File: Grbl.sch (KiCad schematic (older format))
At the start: 19 parts, among them P1 CTL, P2 MISC, P3 STEP, P4 SPIN, P5 LIMIT

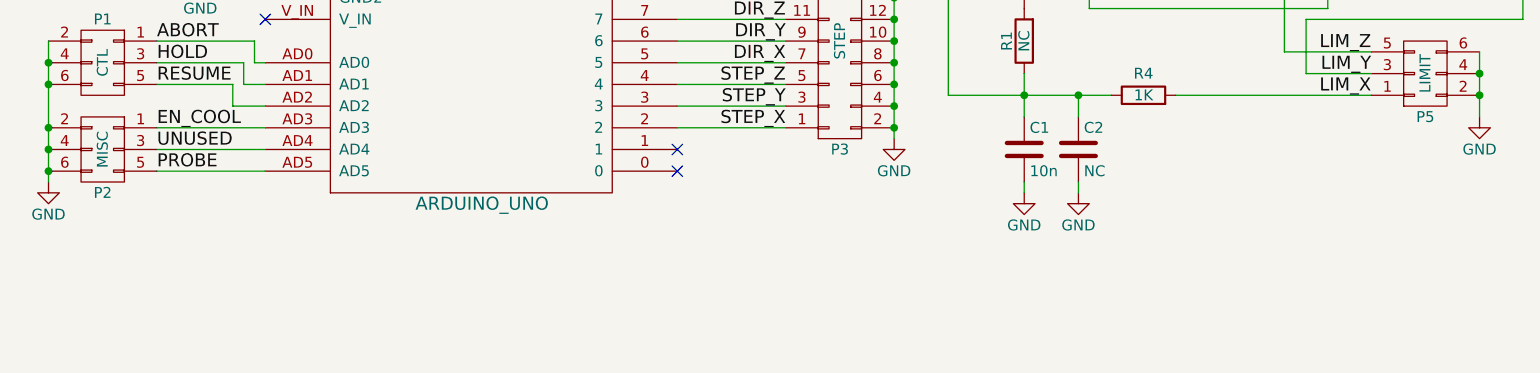
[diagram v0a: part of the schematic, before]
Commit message: Add more ground pins
This helps connecting the shield wire of cables.
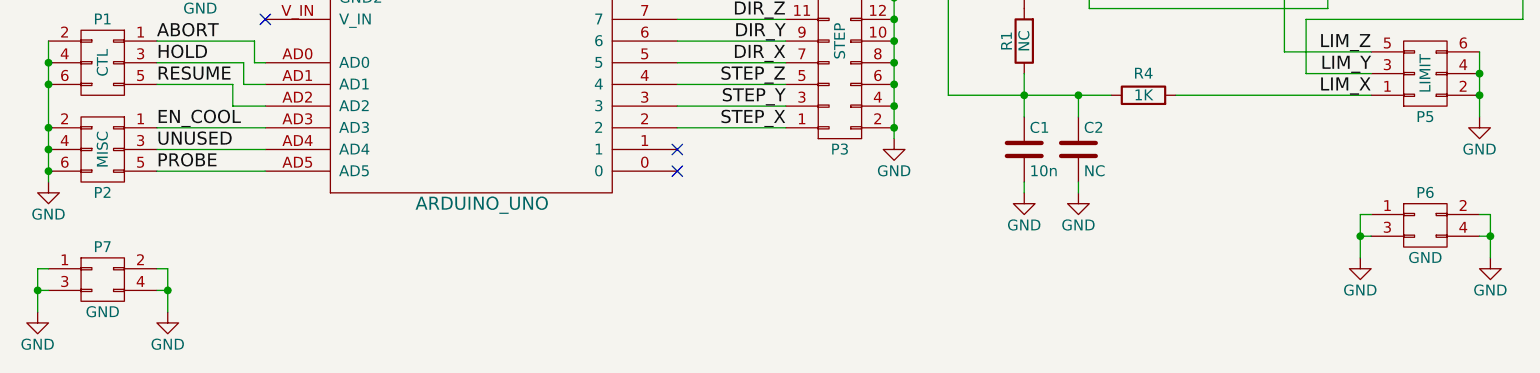
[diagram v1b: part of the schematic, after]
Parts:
- added P6, P7: GND, Pin_Headers:Pin_Header_Straight_2x02, symbol CONN_02X02
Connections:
- net GND: now also P6.1 (P1), P6.2 (P2), P6.3 (P3), P6.4 (P4), P7.1 (P1), P7.2 (P2), P7.3 (P3), P7.4 (P4)
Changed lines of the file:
@@
 NoConn ~ 5750 3300
 $Comp
-L GND #PWR?
+L GND #PWR016
 U 1 1 5638B3BA
 P 5650 1400
-F 0 "#PWR?" H 5650 1150 50  0001 C CNN
+F 0 "#PWR016" H 5650 1150 50  0001 C CNN
 F 1 "GND" H 5650 1250 50  0000 C CNN
 F 2 "" H 5650 1400 60  0000 C CNN
@@
 	3750 2500 3750 2400
 Connection ~ 3750 2400
+$Comp
+L CONN_02X02 P7
+U 1 1 595F1AB2
+P 3100 3800
+F 0 "P7" H 3100 3950 50  0000 C CNN
+F 1 "GND" H 3100 3650 50  0000 C CNN
+F 2 "Pin_Headers:Pin_Header_Straight_2x02" H 3100 2600 50  0001 C CNN
+F 3 "" H 3100 2600 50  0001 C CNN
+	1    3100 3800
+	1    0    0    -1
+$EndComp
+$Comp
+L GND #PWR017
+U 1 1 595F1C99
+P 3400 3950
+F 0 "#PWR017" H 3400 3700 50  0001 C CNN
+F 1 "GND" H 3400 3800 50  0000 C CNN
+F 2 "" H 3400 3950 60  0000 C CNN
+F 3 "" H 3400 3950 60  0000 C CNN
+	1    3400 3950
+	1    0    0    -1
+$EndComp
+$Comp
+L GND #PWR018
+U 1 1 595F1CE0
+P 2800 3950
+F 0 "#PWR018" H 2800 3700 50  0001 C CNN
+F 1 "GND" H 2800 3800 50  0000 C CNN
+F 2 "" H 2800 3950 60  0000 C CNN
+F 3 "" H 2800 3950 60  0000 C CNN
+	1    2800 3950
+	1    0    0    -1
+$EndComp
+Wire Wire Line
+	2800 3750 2800 3950
+Wire Wire Line
+	2800 3850 2850 3850
+Wire Wire Line
+	2800 3750 2850 3750
+Connection ~ 2800 3850
+Wire Wire Line
+	3350 3850 3400 3850
+Wire Wire Line
+	3400 3750 3400 3950
+Wire Wire Line
+	3350 3750 3400 3750
+Connection ~ 3400 3850
+$Comp
+L CONN_02X02 P6
+U 1 1 595F38E7
+P 9200 3550
+F 0 "P6" H 9200 3700 50  0000 C CNN
+F 1 "GND" H 9200 3400 50  0000 C CNN
+F 2 "Pin_Headers:Pin_Header_Straight_2x02" H 9200 2350 50  0001 C CNN
+F 3 "" H 9200 2350 50  0001 C CNN
+	1    9200 3550
+	1    0    0    -1
+$EndComp
+$Comp
+L GND #PWR?
+U 1 1 595F38ED
+P 9500 3700
+F 0 "#PWR?" H 9500 3450 50  0001 C CNN
+F 1 "GND" H 9500 3550 50  0000 C CNN
+F 2 "" H 9500 3700 60  0000 C CNN
+F 3 "" H 9500 3700 60  0000 C CNN
+	1    9500 3700
+	1    0    0    -1
+$EndComp
+$Comp
+L GND #PWR?
+U 1 1 595F38F3
+P 8900 3700
+F 0 "#PWR?" H 8900 3450 50  0001 C CNN
+F 1 "GND" H 8900 3550 50  0000 C CNN
+F 2 "" H 8900 3700 60  0000 C CNN
+F 3 "" H 8900 3700 60  0000 C CNN
+	1    8900 3700
+	1    0    0    -1
+$EndComp
+Wire Wire Line
+	8900 3500 8900 3700
+Wire Wire Line
+	8900 3600 8950 3600
+Wire Wire Line
+	8900 3500 8950 3500
+Connection ~ 8900 3600
+Wire Wire Line
+	9450 3600 9500 3600
+Wire Wire Line
+	9500 3500 9500 3700
+Wire Wire Line
+	9450 3500 9500 3500
+Connection ~ 9500 3600
 $EndSCHEMATC

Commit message: Convert design to KiCad 5, with some changes
This converts the design to use the newer KiCad 5 symbols and
footprints, but additionally makes some changes:
 - The Arduino Uno symbol is now one from the default library instead of a
   third-party symbol, but it has a different pin numbering and layout.
 - The limit pin filtering schematic is a bit more spaced out, using net
   labels instead of direct connections.
 - The Arduino Uno footprint is now one from the default library and has
   two extra pins. It also has smaller mounting holes, see
   https://github.com/KiCad/kicad-footprints/issues/590
 - The solder jumper used was not available anymore, so a bigger one was
   used instead.
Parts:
- C1, C2, C3, C4, C5, C6: footprint Capacitors_SMD:C_0805_HandSoldering -> Capacitor_SMD:C_0805_2012Metric; symbol C -> Device:C
- JP1: footprint Footprints:S_JUMPER_3 -> Jumper:SolderJumper-3_P2.0mm_Open_TrianglePad1.0x1.5mm_NumberLabels; symbol JUMPER3 -> Jumper:SolderJumper_3_Open
- P1, P2, P4, P5: footprint Pin_Headers:Pin_Header_Straight_2x03 -> Connector_PinHeader_2.54mm:PinHeader_2x03_P2.54mm_Vertical; symbol CONN_02X03 -> Connector_Generic:Conn_02x03_Odd_Even
- P3: footprint Pin_Headers:Pin_Header_Straight_2x09 -> Connector_PinHeader_2.54mm:PinHeader_2x09_P2.54mm_Vertical; symbol CONN_02X09 -> Connector_Generic:Conn_02x09_Odd_Even
- P6, P7: footprint Pin_Headers:Pin_Header_Straight_2x02 -> Connector_PinHeader_2.54mm:PinHeader_2x02_P2.54mm_Vertical; symbol CONN_02X02 -> Connector_Generic:Conn_02x02_Odd_Even
- R1, R2, R3, R4, R5, R6: footprint Discret:R3 -> Resistor_THT:R_Axial_DIN0207_L6.3mm_D2.5mm_P7.62mm_Horizontal; symbol R -> Device:R
- SHIELD1: footprint Arduino:ARDUINO_SHIELD -> Module:Arduino_UNO_R2_WithMountingHoles; symbol ARDUINO_UNO -> MCU_Module:Arduino_UNO_R2
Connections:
- net labels added: LIM_X_FILTERED, LIM_Y_FILTERED, LIM_Z_FILTERED
- wire segments 95 -> 105
- no-connect marks 6 -> 7
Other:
- moved on the sheet: C1, C2, C3, C4, C5, C6, R1, R2, R3, R4, R5, R6
